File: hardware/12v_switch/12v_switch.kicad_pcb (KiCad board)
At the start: 2 copper layers, 71.1 x 88.9 mm, 51 parts, among them J1 MOLEX_0530470810, M1 SCREW_6-32_POWER, M11 SCREW_6-32_POWER, M12 SCREW_6-32_POWER, M13 SCREW_6-32_POWER, M14 SCREW_6-32_POWER, M19 SCREW_6-32_NORMAL, M2 SCREW_6-32_POWER, M20 SCREW_6-32_NORMAL, M21 SCREW_6-32_NORMAL, M22 SCREW_6-32_NORMAL, M3 SCREW_6-32_POWER, M4 SCREW_6-32_POWER, M5 SCREW_6-32_POWER, M6 SCREW_6-32_POWER, Q1 INFINEON_IRF7470TRPBF, Q2 INFINEON_IRF7470TRPBF, Q3 INFINEON_IRF7470TRPBF, Q4 INFINEON_IRF7470TRPBF, U1 TI_LM5111-1MX_NOPB, U2 TI_LM5111-1MX_NOPB, U3 TI_LM22680QMRE-ADJ

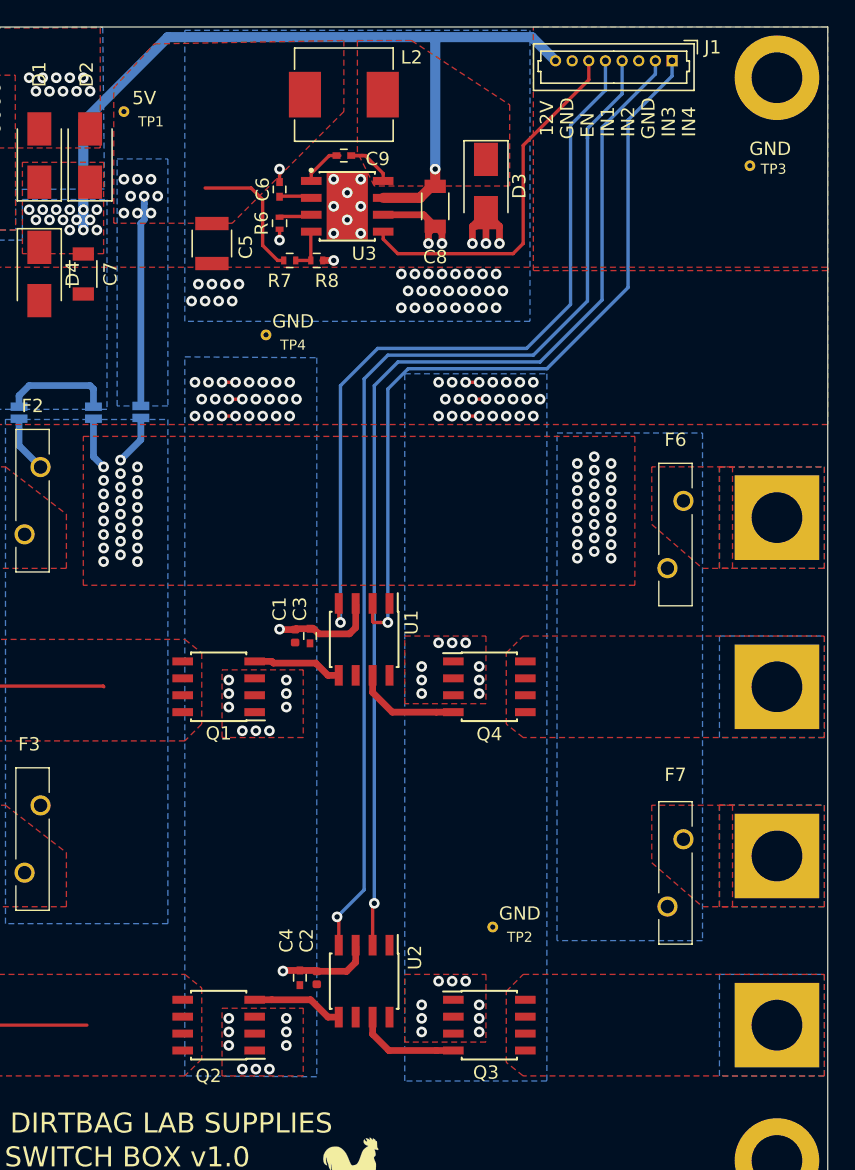
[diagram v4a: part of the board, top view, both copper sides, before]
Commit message: Added separate 5V gate driver LDO
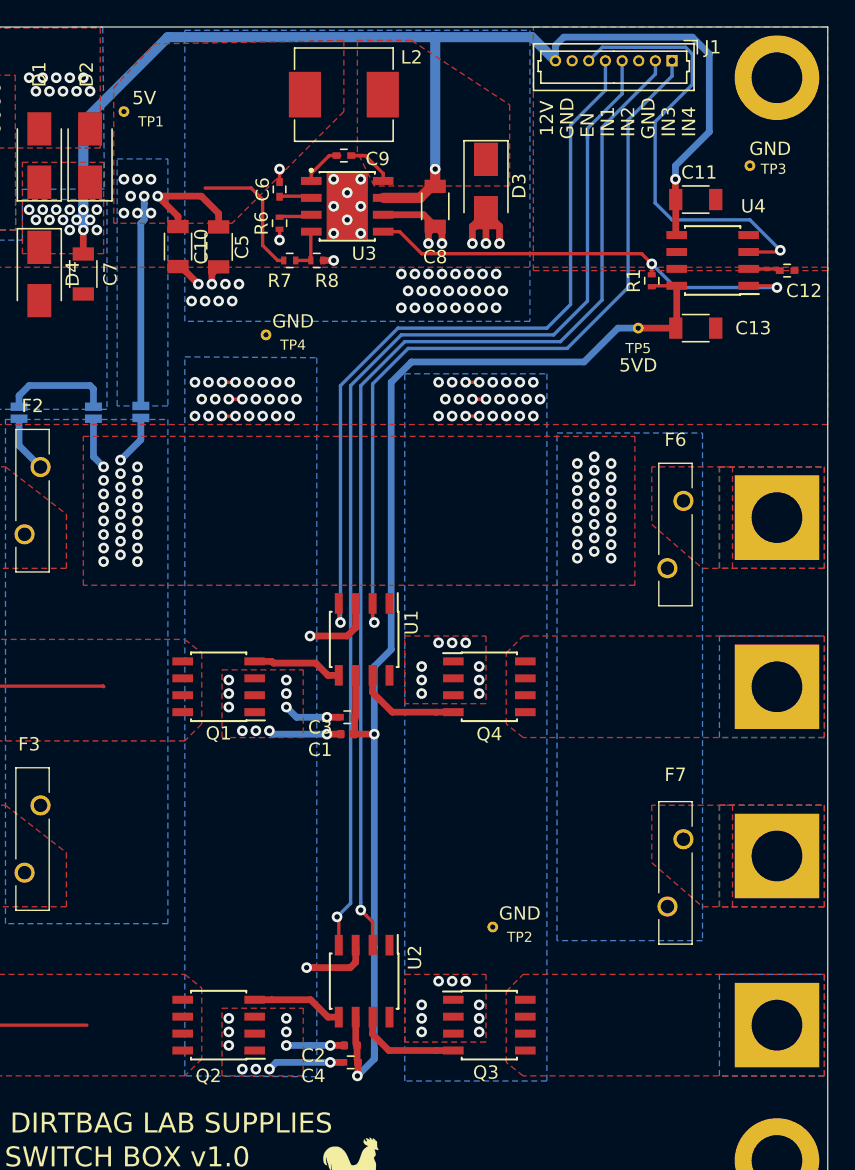
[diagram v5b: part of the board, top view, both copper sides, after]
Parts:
- added C10: MURATA_GRT31CR61H106KE01L, Capacitors_SMD:C_1206, F.Cu at (47.8, 41.9)
- added C11: MURATA_GRT31CR61H106KE01L, Capacitors_SMD:C_1206, F.Cu at (86.6, 38.4)
- added C12: MURATA_GCM155R71E103KA37D, Capacitors_SMD:C_0402, F.Cu at (93.5, 43.7)
- added C13: MURATA_GRM31CC81E226KE11L, Capacitors_SMD:C_1206, F.Cu at (86.6, 48.0)
- added R1: VISHAYDALE_CRCW0402100KJNEDC, Resistors_SMD:R_0402, F.Cu at (83.3, 44.5)
- added TP5: DBLS_TESTPOINT_NORMAL, DBLS_Misc:DBLS_Testpoint_Normal, F.Cu at (82.3, 48.0)
- added U4: TI_LM9076BMA-5.0, Housings_SOIC:SOIC-8_3.9x4.9mm_Pitch1.27mm, F.Cu at (87.9, 42.9)
- C5: value TAIYO-YUDEN_LMK325ABJ107MM-P -> MURATA_GRM31CC81E226KE11L; footprint Capacitors_SMD:C_1210 -> Capacitors_SMD:C_1206
- moved C1 8.34 mm to (60.5, 78.5), turned to 180 degrees
- moved C4 7.41 mm to (60.7, 103.1), turned to 180 degrees
- moved C3 6.71 mm to (60.5, 77.2), turned to 180 degrees
- moved C2 5.68 mm to (60.7, 101.9), turned to 180 degrees
- moved C5 0.57 mm to (50.8, 41.9)
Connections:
- C1 pad 1: +12V -> +5VD
- C2 pad 1: +12V -> +5VD
- C3 pad 1: +12V -> +5VD
- C4 pad 1: +12V -> +5VD
- J1 pad 6: /5V_ENABLE -> /SYSTEM_ENABLE
- U1 pad 6: +12V -> +5VD
- U2 pad 6: +12V -> +5VD
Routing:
- net +5VD: track 0.00 -> 92.2 mm, vias 0 -> 2
- net /SYSTEM_ENABLE: track 0.00 -> 34.0 mm, vias 0 -> 1
- net +12V: track 70.6 -> 100.5 mm, vias 15 -> 16
- net GND: track 39.2 -> 58.3 mm, vias 126 -> 138
- net +5V: track 26.0 -> 35.1 mm
- net /5V_ENABLE: track 27.6 -> 34.3 mm, vias 0 -> 2
- net Net-(C12-Pad1): track 0.00 -> 2.39 mm
- net /PWM3: track 81.4 -> 82.8 mm
- net (no net): vias 8 -> 0
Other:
- board text added: "5VD"

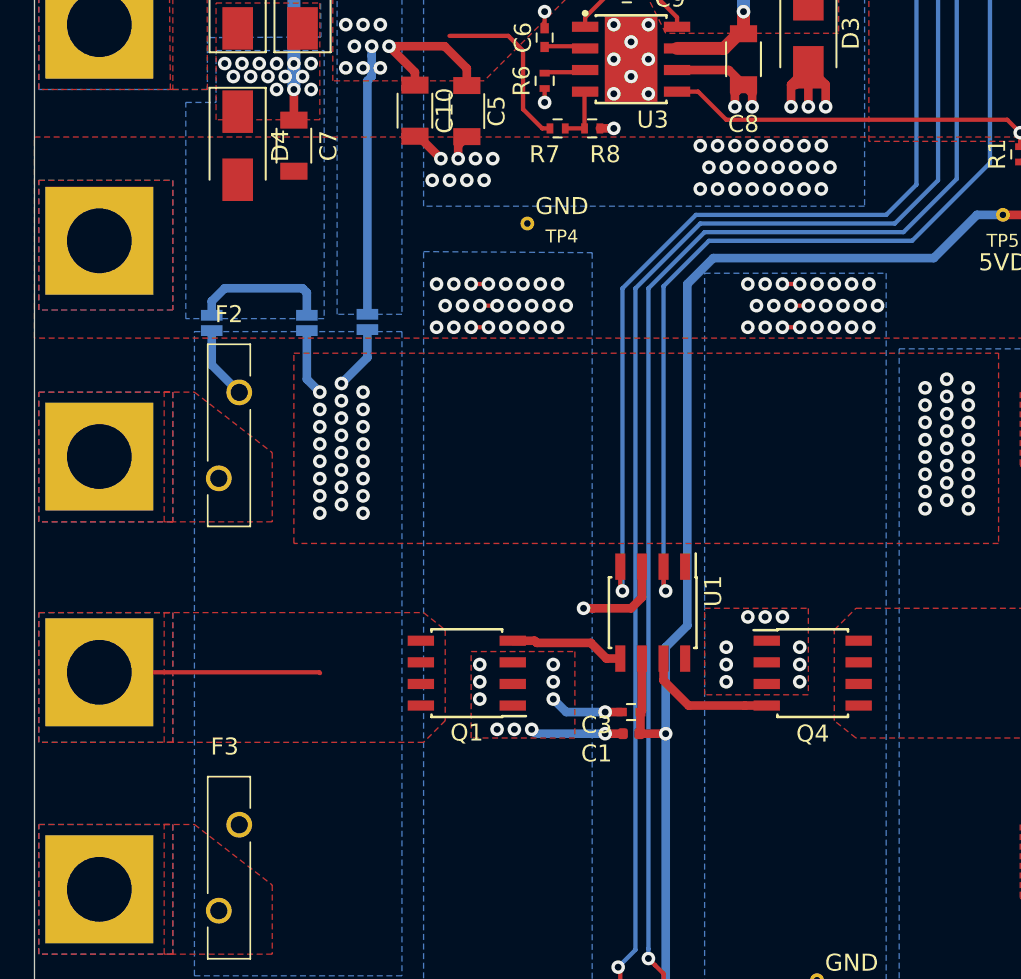
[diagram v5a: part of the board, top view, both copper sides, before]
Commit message: added cad files for FreeCAD 0.19
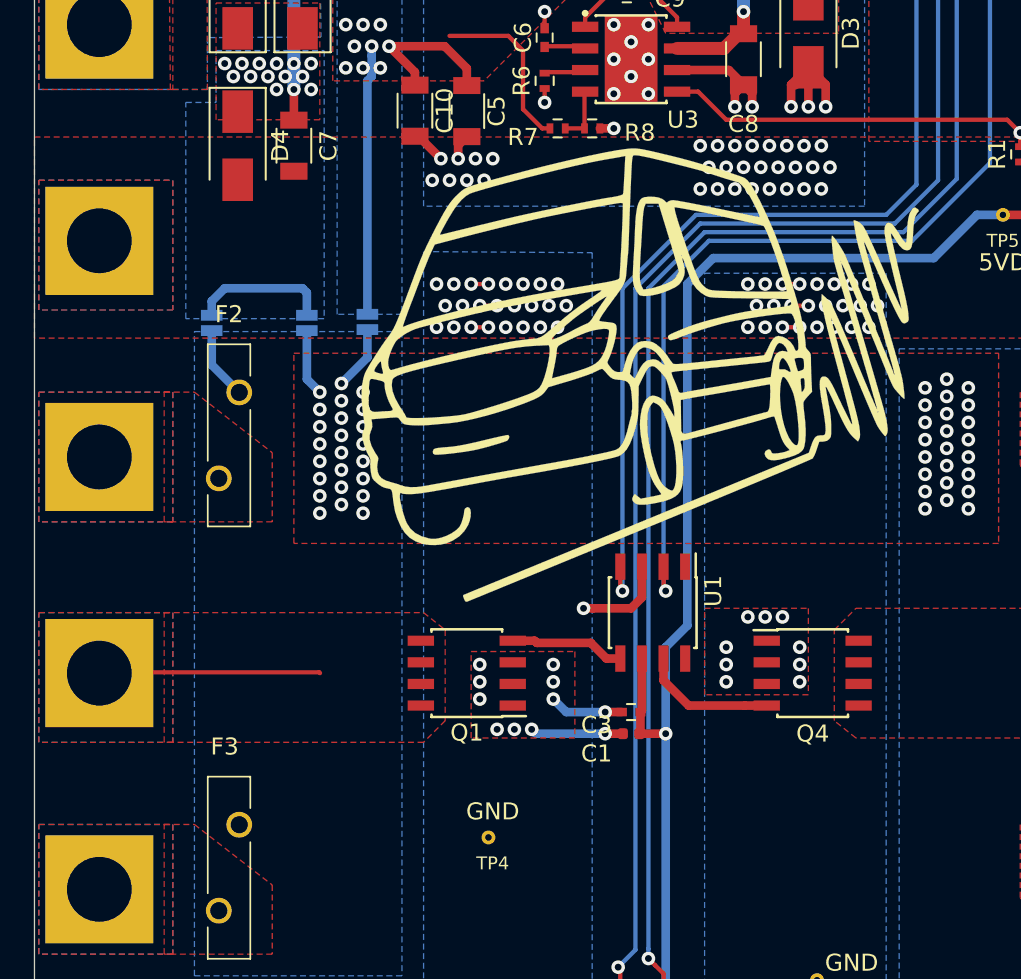
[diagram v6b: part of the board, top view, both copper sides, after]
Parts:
- added LOGO2: DBLS_Chicken_Large, DBLS_LOGO:Rooster_43mmx43mm, B.Cu at (60.7, 70.6)
- added LOGO4: DBLS_van_logo_small_v1, DBLS_LOGO:van_logo_small, F.Cu at (61.0, 57.4)
- C6: value MURATA_GCM155R71C104KA55J -> MURATA_GRM155R71H104ME14J
- moved TP4 36.1 mm to (52.1, 84.6)
